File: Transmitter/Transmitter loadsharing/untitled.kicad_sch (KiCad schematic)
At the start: 22 parts, among them U2 THS3091D, U3 THS3091D, U4 THS3091D, U5 THS3091D, U6 THS3091D, U7 THS3091D

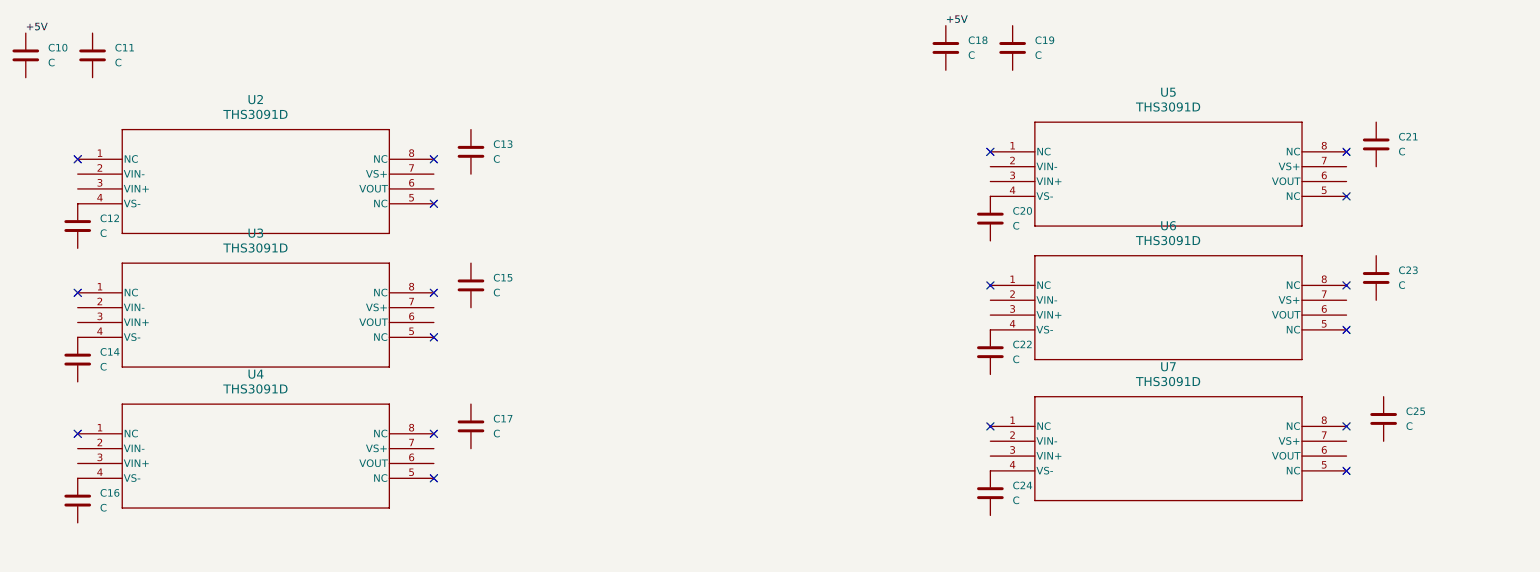
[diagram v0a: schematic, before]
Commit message: mostly changes to transmitter prototype, for using the prototyper
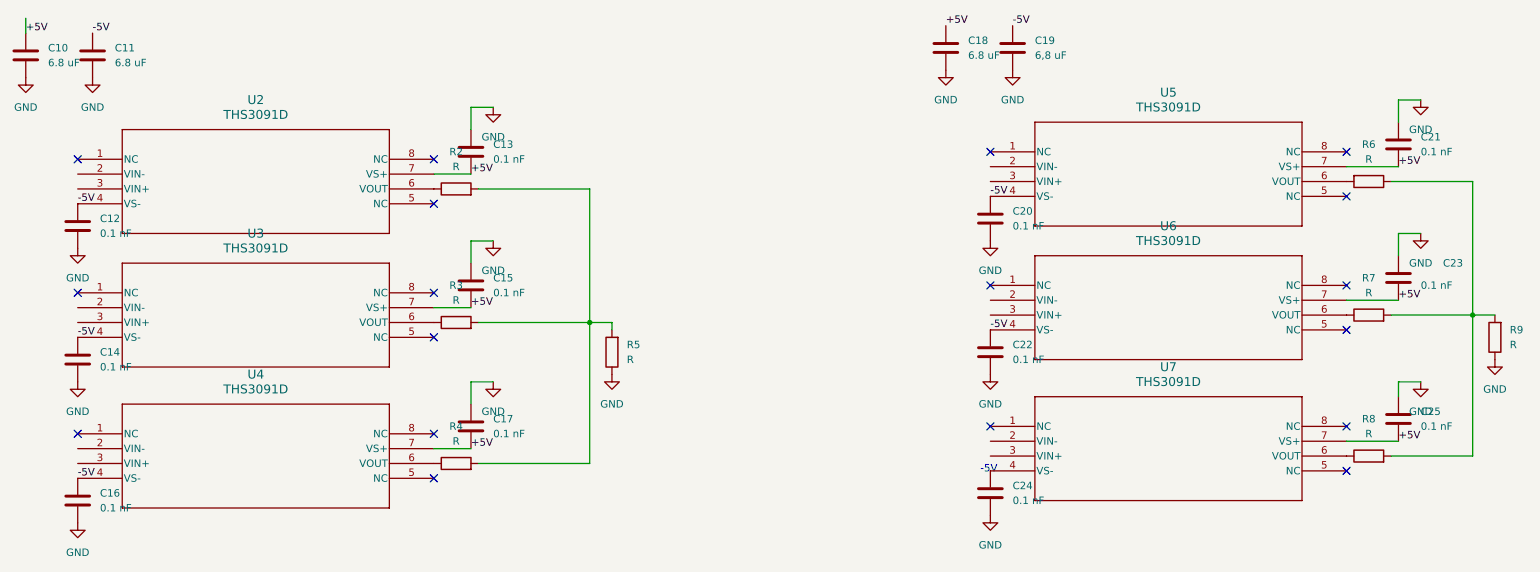
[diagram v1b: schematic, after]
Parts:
- added R2, R3, R4, R5, R6, R7, R8, R9: R, symbol Device:R
- C10, C11, C18: value C -> 6.8 uF
- C12, C13, C14, C15, C16, C17, C20, C21, C22, C23, C24, C25: value C -> 0.1 nF
- C19: value C -> 6,8 uF
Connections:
- net +5V: now also C13.2, C15.2, C17.2, C21.2, C23.2, C25.2, U2.7 (VS+), U3.7 (VS+), U4.7 (VS+), U5.7 (VS+), U6.7 (VS+), U7.7 (VS+)
- net GND: now reaches C24.2
- net GND: now also C10.2, C11.2, C12.2, C13.1, C14.2, C15.1, C16.2, C17.1, C18.2, C19.2, C20.2, C21.1, C22.2, C23.1, C25.1, R5.1, R9.1
- net -5V: now reaches C14.1, U3.4 (VS-)
- net -5V: now also C11.1, C12.1, C16.1, C19.1, C20.1, C22.1, U2.4 (VS-), U4.4 (VS-), U5.4 (VS-), U6.4 (VS-)
- net at U4.6 (VOUT): now also R4.1
- net at U7.6 (VOUT): now also R8.1
- net at U3.6 (VOUT): now also R3.1
- net at U2.6 (VOUT): now also R2.1
- net at U6.6 (VOUT): now also R7.1
- net at U5.6 (VOUT): now also R6.2
- new net: R2.2, R3.2, R4.2, R5.2
- new net: R6.1, R7.2, R8.2, R9.2
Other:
- note added: "-5V"
- moved on the sheet: C21, C23, C25
